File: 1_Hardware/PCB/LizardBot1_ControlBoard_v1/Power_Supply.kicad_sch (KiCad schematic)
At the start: 47 parts, among them J201 XT60-M, J202 Receptable-P5.08-2P, J203 JST-PH-2-Male, J204 JST-PH-2-Male, J205 Receptable-P5.08-4P, J206 JST-PH-2-Male, J207 USB_C_Receptacle_PowerOnly_6P, Q201 SQ4425EY, SW201 SW_SPDT, U201 MP2225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

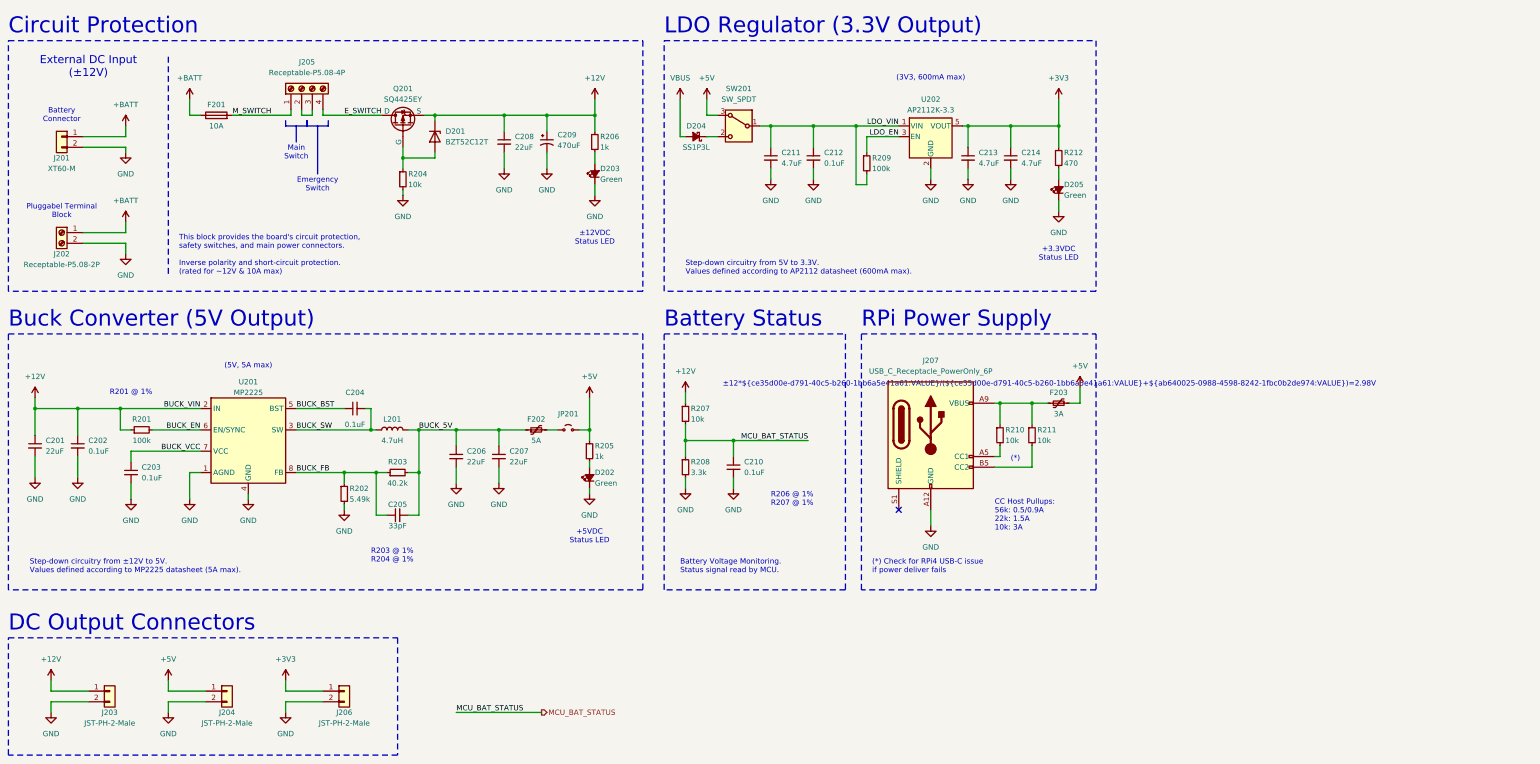
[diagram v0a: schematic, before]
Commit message: Finished PCB routing. Updated ESP32 GPIO layout.
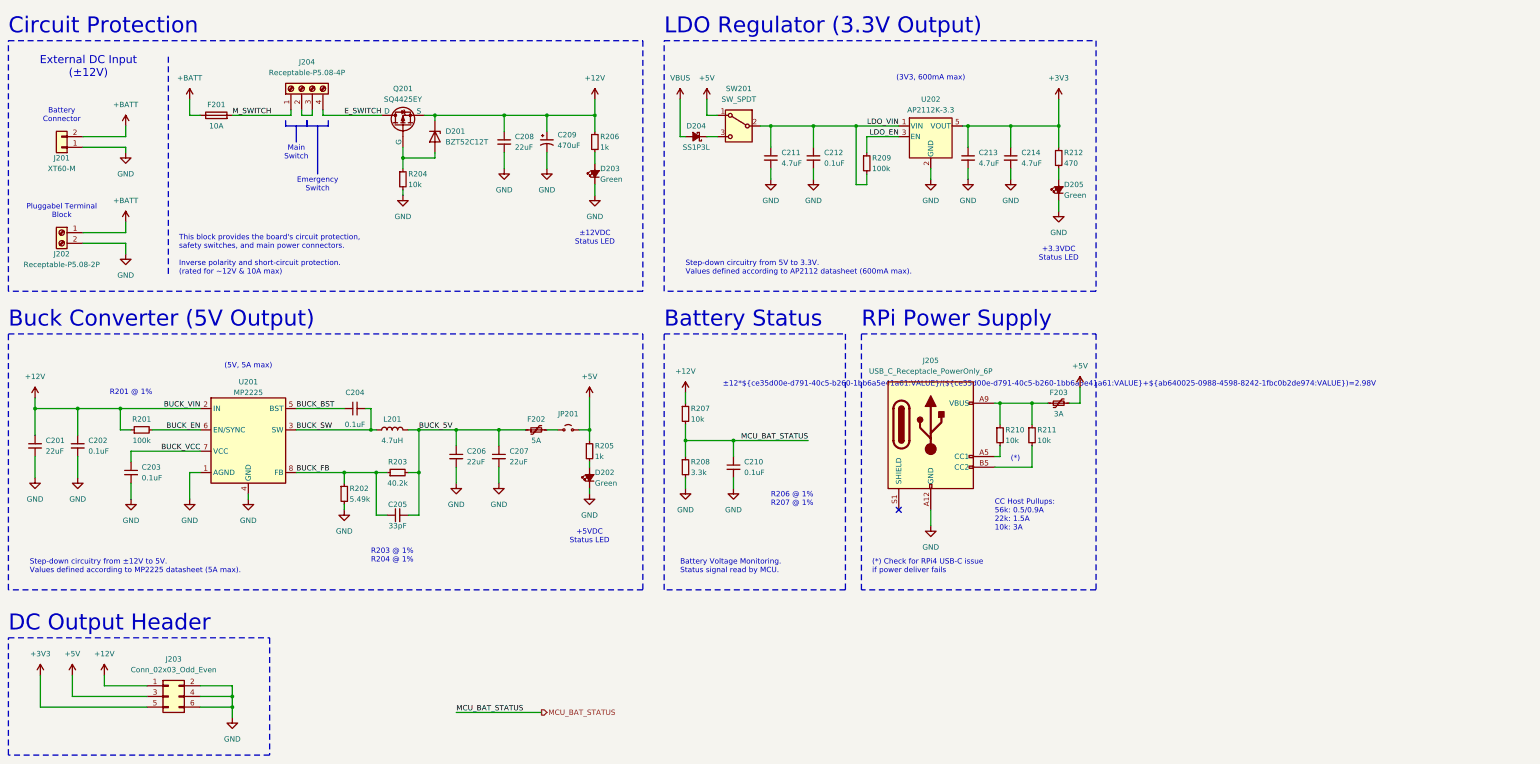
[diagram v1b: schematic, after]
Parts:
- removed J203, J204, J206: JST-PH-2-Male, Connector_JST:JST_PH_S2B-PH-K_1x02_P2.00mm_Horizontal, symbol Connector_Generic:Conn_01x02
- added J203: Conn_02x03_Odd_Even, Connector_PinHeader_2.54mm:PinHeader_2x03_P2.54mm_Vertical, symbol Connector_Generic:Conn_02x03_Odd_Even
- F201: footprint Fuse:Fuseholder_Clip-5x20mm_Littelfuse_519_Inline_P20.60x5.00mm_D1.00mm_Horizontal -> Project_FootprintLib:Fuseholder_LittelFuse_5x20mm_0PTF0078P
- JP201: now left out of the parts list
- SW201: symbol Switch:SW_SPDT_312 -> Switch:SW_SPDT
- renumbered J205 to J204, J207 to J205
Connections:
- net +12V: now also J203.1 (Pin_1)
- net +3V3: now also J203.5 (Pin_5)
- net +5V: now also SW201.1 (A), J203.3 (Pin_3); no longer SW201.3 (A)
- net +BATT: now also J201.2 (Pin_2); no longer J201.1 (Pin_1)
- net GND: now also J201.1 (Pin_1), J203.2 (Pin_2), J203.4 (Pin_4), J203.6 (Pin_6); no longer J201.2 (Pin_2)
- net LDO_VIN: now also SW201.2 (B); no longer SW201.1 (B)
- net at D204.1 (K): now also SW201.3 (C); no longer SW201.2 (C)
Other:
- note added: "DC Output Header"
- note removed: "DC Output Connectors"
- moved on the sheet: J201
